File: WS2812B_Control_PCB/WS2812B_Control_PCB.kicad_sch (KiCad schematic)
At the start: 25 parts, among them J1 TB002-500-02BE, J2 TB002-500-02BE, J3 Conn_01x05, J4 S3B-XH-ALFSN, J5 S3B-XH-ALFSN, J6 S3B-XH-ALFSN, J7 S3B-XH-ALFSN, J8 S3B-XH-ALFSN, U1 IRM-20-5, U2 113991254, U3 MC74VHCT50ADTR2G

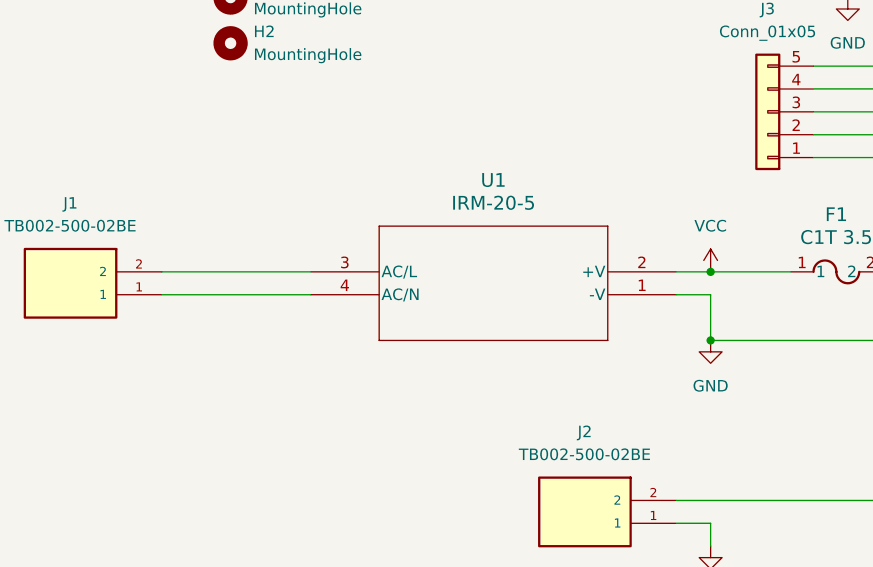
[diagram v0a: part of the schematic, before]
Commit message: Fixed flaw in v1. Pinout of IRM-20-5 was incorrect. Corrected.
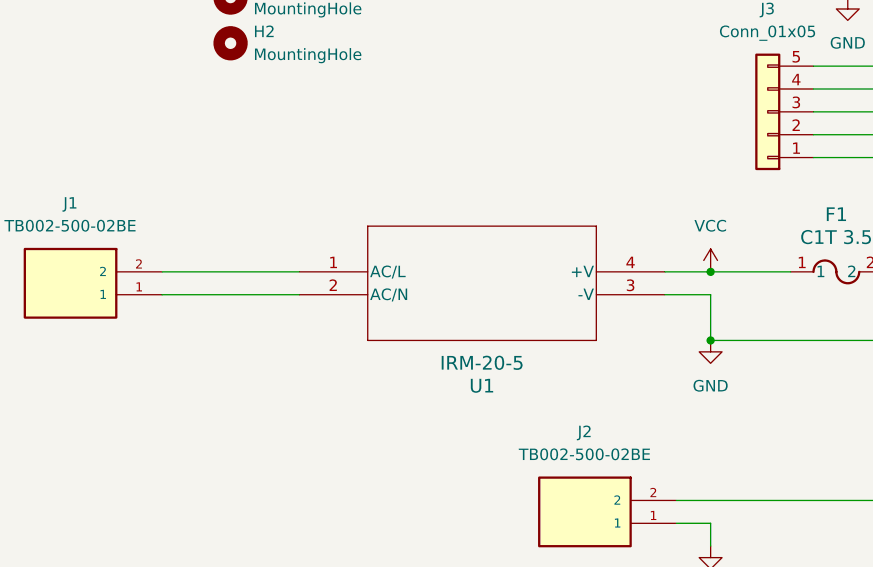
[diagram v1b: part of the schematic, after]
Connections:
- net GND: now also U1.3 (-V); no longer U1.1 (-V)
- net VCC: now also U1.4 (+V); no longer U1.2 (+V)
- net at J1.1: now also U1.2 (AC/N); no longer U1.4 (AC/N)
- net at J1.2: now also U1.1 (AC/L); no longer U1.3 (AC/L)
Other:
- moved on the sheet: U1
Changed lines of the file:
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@@
 	(wire
 		(pts
-			(xy 53.34 90.17) (xy 69.85 90.17)
+			(xy 53.34 90.17) (xy 68.58 90.17)
 		)
 		(stroke
@@
 	(wire
 		(pts
+			(xy 109.22 92.71) (xy 114.3 92.71)
+		)
+		(stroke
+			(width 0)
+			(type default)
+		)
+	)
+	(wire
+		(pts
 			(xy 153.67 90.17) (xy 153.67 92.71)
 		)
@@
 	(wire
 		(pts
-			(xy 53.34 92.71) (xy 69.85 92.71)
+			(xy 53.34 92.71) (xy 68.58 92.71)
 		)
 		(stroke
@@
 	(wire
 		(pts
+			(xy 114.3 92.71) (xy 114.3 97.79)
+		)
+		(stroke
+			(width 0)
+			(type default)
+		)
+	)
+	(wire
+		(pts
 			(xy 153.67 123.19) (xy 154.94 123.19)
 		)
@@
 	(wire
 		(pts
-			(xy 110.49 90.17) (xy 114.3 90.17)
+			(xy 109.22 90.17) (xy 114.3 90.17)
 		)
 		(stroke
@@
 	(wire
 		(pts
-			(xy 114.3 92.71) (xy 110.49 92.71)
-		)
-		(stroke
-			(width 0)
-			(type default)
-		)
-	)
-	(wire
-		(pts
 			(xy 149.86 48.26) (xy 152.4 48.26)
 		)
@@
 		)
 	)
-	(wire
-		(pts
-			(xy 114.3 97.79) (xy 114.3 92.71)
-		)
-		(stroke
-			(width 0)
-			(type default)
-		)
-	)
 	(symbol
 		(lib_id "WS2812Board:113991254")
@@
 	(symbol
 		(lib_id "WS2812Board:IRM-20-5")
-		(at 110.49 92.71 180)
+		(at 68.58 90.17 0)
 		(unit 1)
 		(body_style 1)
@@
 		(dnp no)
 		(property "Reference" "U1"
-			(at 90.17 80.01 0)
+			(at 88.9 102.87 0)
 			(show_name no)
 			(do_not_autoplace no)
@@
 		)
 		(property "Value" "IRM-20-5"
-			(at 90.17 82.55 0)
+			(at 88.9 100.33 0)
 			(show_name no)
 			(do_not_autoplace no)
@@
 		)
 		(property "Footprint" "WS2812Board:CONV_IRM-20-5"
-			(at 110.49 92.71 0)
+			(at 68.58 90.17 0)
 			(hide yes)
 			(show_name no)
@@
 		)
 		(property "Datasheet" "IRM-20-5"
-			(at 110.49 92.71 0)
+			(at 68.58 90.17 0)
 			(hide yes)
 			(show_name no)
@@
 		)
 		(property "Description" "AC/DC CONVERTER 5V 20W"
-			(at 110.49 92.71 0)
+			(at 68.58 90.17 0)
 			(hide yes)
 			(show_name no)
